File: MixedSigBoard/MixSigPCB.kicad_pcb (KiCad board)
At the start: 4 copper layers, 58.3 x 75.8 mm, 114 parts, among them J200 2x5 1.27mm, J201 USB_C_Receptacle_USB2.0, J300 031-5640-1010, J400 031-5640-1010, U100 TLV62569DBV, U101 HT7533-1, U102 MCP6001T-E/OT, U200 STM32F103CBT6, U201 USBLC6-2SC6, U300 REF3033AIDBZT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

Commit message: add DAC routing, power routing, finish routing
- finished routing, cleared up most DRC errors
- Removed reference designators on F. Silkscreen
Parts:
- J300, J400: footprint MixSig_Footprints_KiCad6:AMPHENOL-BNC-031-5640-1010 -> MixSig_Footprints.pretty:AMPHENOL-BNC-031-5640-1010
- L101: footprint MixSig_Footprints_KiCad6:MWSA0603S -> MixSig_Footprints.pretty:MWSA0603S
- L201: footprint MixSig_Footprints_KiCad6:CMC-1206 -> MixSig_Footprints.pretty:CMC-1206
- U301, U400: footprint MixSig_Footprints_KiCad6:VSSOP-10 -> MixSig_Footprints.pretty:VSSOP-10
- moved D200 29.6 mm to (31.4, 42.5), turned to -90 degrees
- moved C203 26.4 mm to (31.3, 39.5), turned to 0 degrees
- moved R201 24.7 mm to (36.3, 44.0), turned to 180 degrees
- moved R202 24.5 mm to (36.3, 45.5), turned to 180 degrees
- moved R200 20.4 mm to (36.3, 41.0), turned to 180 degrees
- moved C301 10.5 mm to (35.2, 51.0)
- moved R405 6.86 mm to (67.3, 70.0), turned to 90 degrees
- moved C210 6.85 mm to (50.6, 19.8)
- moved D201 6.85 mm to (58.1, 22.6)
- moved D202 6.85 mm to (58.3, 28.0)
- moved D203 6.85 mm to (55.6, 31.0)
- moved D204 6.85 mm to (51.9, 31.0)
- moved D205 6.85 mm to (48.2, 28.2)
- moved J200 6.85 mm to (53.1, 25.3)
- moved R207 6.85 mm to (58.3, 31.0)
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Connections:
- R201 pad 1: /MCU/TIM4_CH1 -> /MCU/TIM4_CH2
- R202 pad 1: /MCU/TIM4_CH2 -> /MCU/TIM4_CH1
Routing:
- net +3V3: track 18.8 -> 195.4 mm, vias 0 -> 16
- net +5V: track 7.08 -> 84.7 mm, vias 0 -> 5
- net +3.3VA: track 27.6 -> 80.4 mm, vias 0 -> 2
- net /MCU/NRST: track 6.29 -> 28.7 mm, vias 0 -> 2
- net /MCU/TIM4_CH1: track 5.83 -> 26.9 mm, vias 0 -> 2
- net /MCU/TIM4_CH2: track 5.36 -> 25.4 mm, vias 0 -> 2
- net /MCU/TIM4_CH3: track 4.87 -> 24.6 mm, vias 0 -> 2
- net GND: track 63.0 -> 53.1 mm, vias 69 -> 98
- net /MCU/SWO: track 15.5 -> 7.37 mm, vias 2 -> 0
- net /MCU/SWDIO: track 21.1 -> 14.0 mm, vias 2 -> 0
- net /MCU/SWCLK: track 14.7 -> 7.65 mm, vias 2 -> 0
- net /DAC/OUT: track 1.04 -> 7.29 mm
- net /Power/BUCK_SW: track 6.77 -> 0.89 mm
- net /Power/+5V_FILT: track 2.36 -> 7.37 mm
- net /DAC/OUT_AA_BUF_OUT: track 3.81 -> 8.14 mm
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- added copper zone on F.Cu, net /Power/+5V_FILT
- added copper zone on F.Cu, net /Power/BUCK_SW
- removed copper zone on F.Cu, net /ADC/ADC_VREF
- removed copper zone on F.Cu, net /DAC/DAC_VREF
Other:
- board size 58.3 x 75.8 mm -> 59.9 x 73.3 mm
- board text removed: "Route essentials (high speed, decoupling caps, signals), then power"

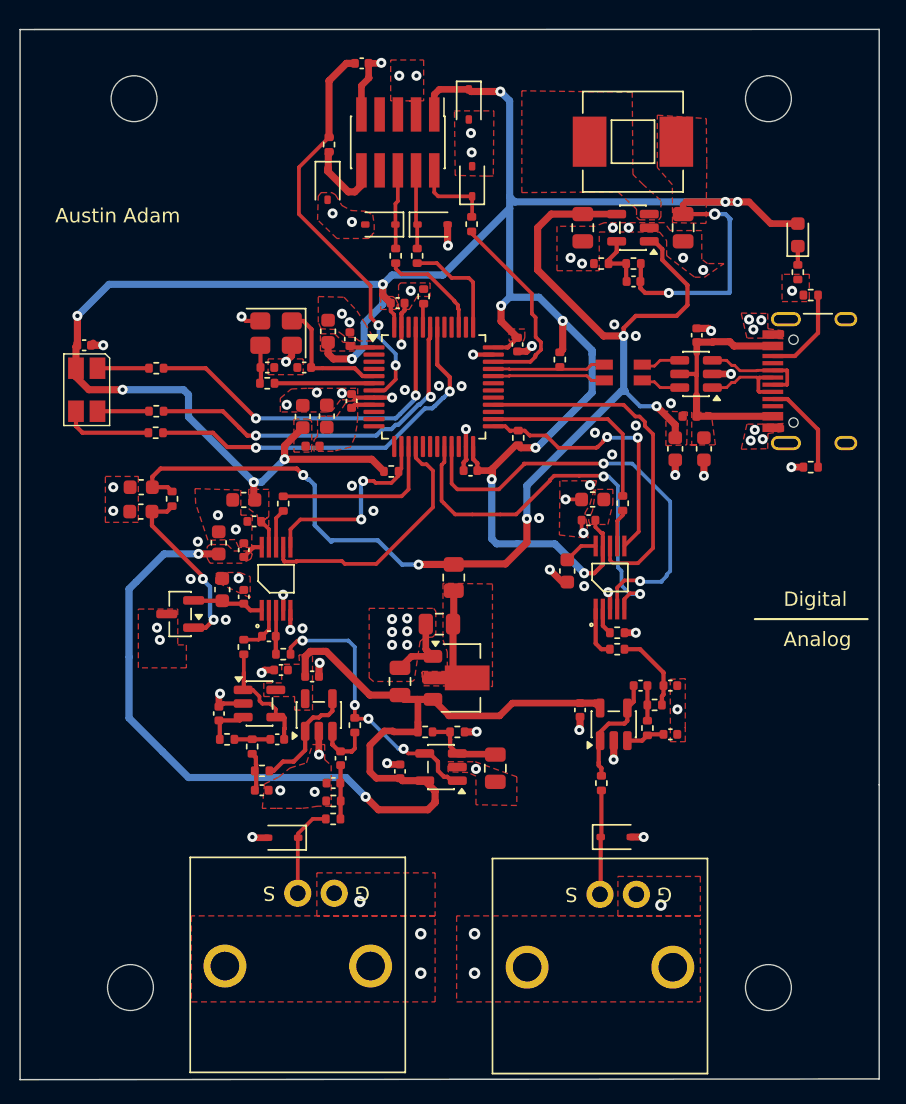
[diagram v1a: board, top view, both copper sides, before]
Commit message: Add missing footprints
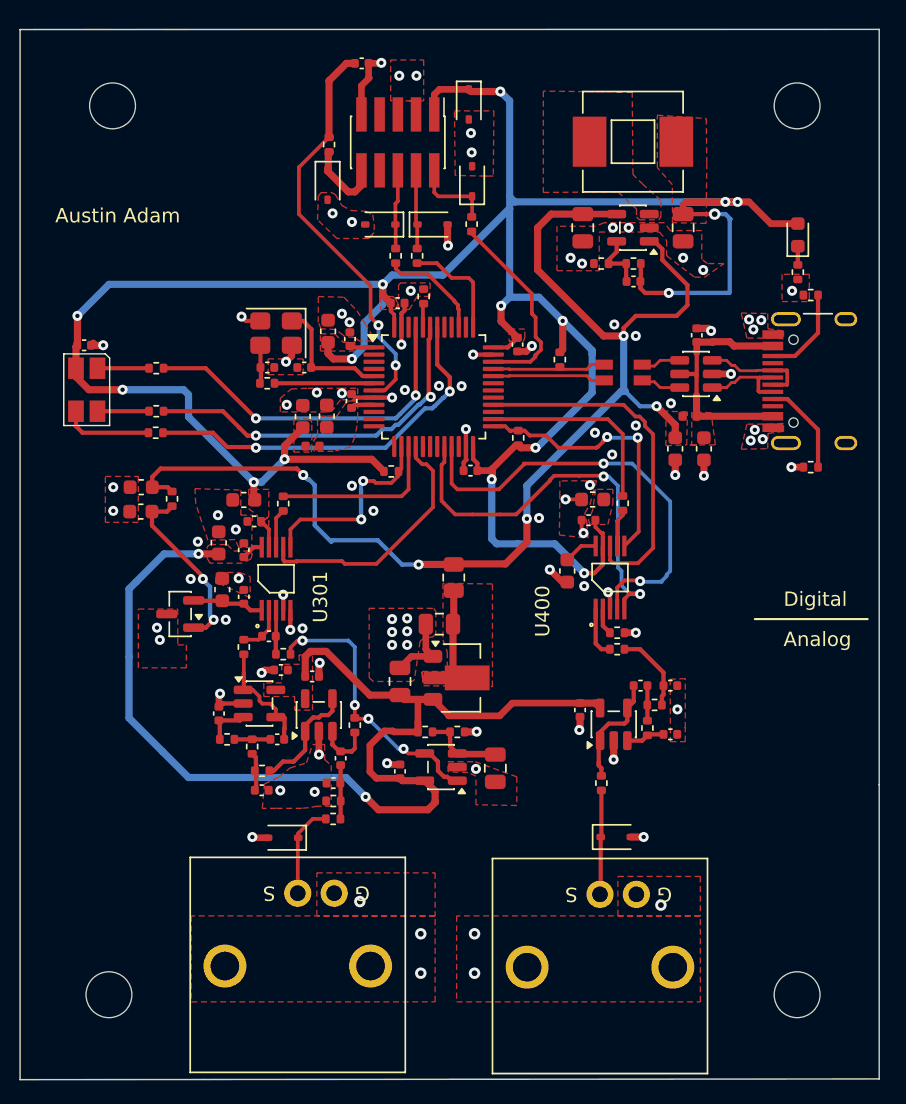
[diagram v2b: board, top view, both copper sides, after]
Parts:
- U301, U400: footprint MixSig_Footprints.pretty:VSSOP-10 -> MixSig_Footprints:VSSOP-10
- moved H3 2.06 mm to (81.0, 22.8)
- moved H4 2.06 mm to (81.0, 84.8)
- moved H1 1.58 mm to (33.0, 84.8)
- moved H2 1.58 mm to (33.2, 22.8)
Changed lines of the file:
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@@
 			)
 		)
-		(fp_text user "${REF}"
+		(fp_text user "J300"
 			(at 0 7.5 180)
 			(unlocked yes)
@@
 		)
 		(embedded_fonts no)
-		(model "C:/Users/phili/OneDrive/Electrical/STEP FILES/BNC-31-5640-1010.stp"
+		(model "${KIPRJMOD}/PCB_Footprints/31-5640-1010.step"
 			(offset
 				(xyz 0 30.15 8)
@@
 	(footprint "MountingHole:MountingHole_3.2mm_M3"
 		(layer "F.Cu")
-		(at 34.75 22.25)
+		(at 33.25 22.75)
 		(descr "Mounting Hole 3.2mm, M3, no annular, generated by kicad-footprint-generator mountinghole.py")
 		(tags "mountinghole M3")
@@
 		)
 	)
-	(footprint "MixSig_Footprints.pretty:VSSOP-10"
+	(footprint "MixSig_Footprints:VSSOP-10"
 		(layer "F.Cu")
 		(at 44.6568 55.7352)
 		(property "Reference" "U301"
-			(at -2.25 0 90)
+			(at 3.0932 1.2648 90)
 			(layer "F.SilkS")
-			(hide yes)
 			(effects
 				(font
@@
 		(sheetname "/ADC/")
 		(sheetfile "ADC.kicad_sch")
-		(attr through_hole)
+		(attr smd)
 		(fp_line
 			(start -1.25 -0.975)
@@
 	(footprint "MountingHole:MountingHole_3.2mm_M3"
 		(layer "F.Cu")
-		(at 34.5 84.25)
+		(at 33 84.75)
 		(descr "Mounting Hole 3.2mm, M3, no annular, generated by kicad-footprint-generator mountinghole.py")
 		(tags "mountinghole M3")
@@
 		(sheetfile "MCU.kicad_sch")
 		(attr smd)
-		(fp_text user "${REF}"
+		(fp_text user "L201"
 			(at 0.625 5.1 0)
 			(unlocked yes)
@@
 		)
 		(embedded_fonts no)
-		(model "C:/Users/phili/OneDrive/Electrical/STEP FILES/CMC-1206.step"
+		(model "${KIPRJMOD}/PCB_Footprints/Coilcraft-1206CS.step"
 			(offset
 				(xyz 0 0 0)
@@
 	(footprint "MountingHole:MountingHole_3.2mm_M3"
 		(layer "F.Cu")
-		(at 79 22.25)
+		(at 81 22.75)
 		(descr "Mounting Hole 3.2mm, M3, no annular, generated by kicad-footprint-generator mountinghole.py")
 		(tags "mountinghole M3")
@@
 			(layer "F.Fab")
 		)
-		(fp_text user "${REF}"
+		(fp_text user "L101"
 			(at 0 7.62 0)
 			(unlocked yes)
@@
 		)
 		(embedded_fonts no)
-		(model "C:/Users/phili/OneDrive/Electrical/STEP FILES/MWSA0603S.STEP"
+		(model "${KIPRJMOD}/PCB_Footprints/IND_MWSA0603S_SNL.step"
 			(offset
 				(xyz 0 0 0)
@@
 		)
 	)
-	(footprint "MixSig_Footprints.pretty:VSSOP-10"
+	(footprint "MixSig_Footprints:VSSOP-10"
 		(layer "F.Cu")
 		(at 67.95 55.65)
 		(property "Reference" "U400"
-			(at -2.25 0 90)
+			(at -4.7 2.35 90)
 			(layer "F.SilkS")
-			(hide yes)
 			(effects
 				(font
@@
 		(sheetname "/DAC/")
 		(sheetfile "DAC.kicad_sch")
-		(attr through_hole)
+		(attr smd)
 		(fp_line
 			(start -1.25 -0.975)
@@
 	(footprint "MountingHole:MountingHole_3.2mm_M3"
 		(layer "F.Cu")
-		(at 79 84.25)
+		(at 81 84.75)
 		(descr "Mounting Hole 3.2mm, M3, no annular, generated by kicad-footprint-generator mountinghole.py")
 		(tags "mountinghole M3")
@@
 			)
 		)
-		(fp_text user "${REF}"
+		(fp_text user "J400"
 			(at 0 7.5 180)
 			(unlocked yes)
@@
 		)
 		(embedded_fonts no)
-		(model "C:/Users/phili/OneDrive/Electrical/STEP FILES/BNC-31-5640-1010.stp"
+		(model "${KIPRJMOD}/PCB_Footprints/31-5640-1010.step"
 			(offset
 				(xyz 0 30.15 8)
@@
 			(pts
 				(xy 71.35 30.7) (xy 71.5 30.5) (xy 71.5 29.35) (xy 70.272013 28.25) (xy 69.549876 27.535716) (xy 69.5 21.8)
-				(xy 61.8 21.7) (xy 61.8 28.8) (xy 68.5 28.75) (xy 69.8 29.95) (xy 69.8 30.5) (xy 70 30.7)
+				(xy 63.3 21.719481) (xy 63.3 28.788806) (xy 68.5 28.75) (xy 69.8 29.95) (xy 69.8 30.5) (xy 70 30.7)
 			)
 		)
@@
 		(polygon
 			(pts
-				(xy 51.45 62.9) (xy 51.15 62.65) (xy 51.15 57.8) (xy 51.15 57.8) (xy 55.65 57.8) (xy 55.8 58) (xy 55.8 59.55)
-				(xy 55.6 59.8) (xy 55 59.85) (xy 54.7 60.1) (xy 54.3 62.8) (xy 54.15 62.9)
+				(xy 51.45 62.9) (xy 51.15 62.65) (xy 51.15 57.8) (xy 55.65 57.8) (xy 55.8 58) (xy 55.8 59.55) (xy 55.6 59.8)
+				(xy 55 59.85) (xy 54.7 60.1) (xy 54.3 62.8) (xy 54.15 62.9)
 			)
 		)

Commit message: Include Gerber and Assembly parts except BOM
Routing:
- net GND: vias 98 -> 356
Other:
- board text added: "ADC"
- board text added: "BW 20Hz - 20kHz"
- board text added: "DAC"
- board text added: "IN"
- board text added: "ON"
- board text added: "OUT"
- board text added: "SWD"
